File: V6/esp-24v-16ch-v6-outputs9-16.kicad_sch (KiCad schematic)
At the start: 5 parts, among them Q12 MMBT2222A

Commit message: V6 is up
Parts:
- R113: renamed from R112; Package 0402/1005 -> (none)
- R114: renamed from R113; value 1k -> 470R; LCSC Part # C11702 -> C25117; Mfr PN 0402WGF1001TCE -> 0402WGF4700TCE; Vendor PN C11702 -> C25117
- renumbered D65 to D66, R114 to R115
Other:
- note added: "I_{BASE} = (3.3V - V_{BE}) / 470R I_{BASE} = (3.3V - 0.7V) / 470R I_{BASE} = 5,53 mA ADEQUATE FOR FULL SATURATION OF THE TRANSISTOR UP TO I_{C} AROUND 550 mA CONSIDERING A FORCED BETA OF 10."

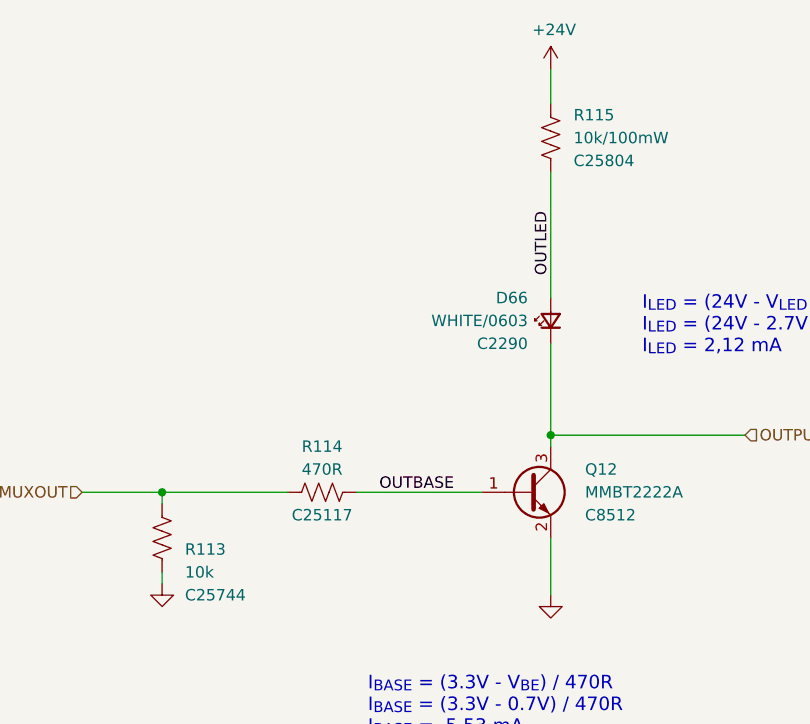
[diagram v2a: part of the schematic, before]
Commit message: Added voltage monitors for both ESP32 and LAN8710A
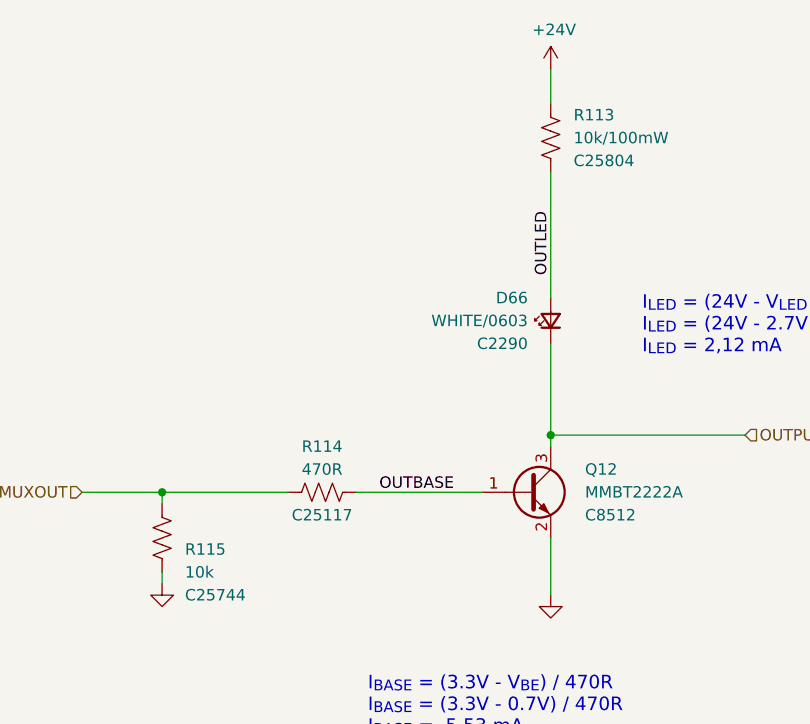
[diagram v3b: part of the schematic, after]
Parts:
- renumbered R115 to R113, R113 to R115
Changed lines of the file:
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@@
 		(title "ESP 24V 16xIn/16xOut/1-Wire Module")
 		(date "2026-02-10")
-		(rev "V6.0")
+		(rev "V6.0.3")
 	)
 	(text "RESISTORS: 62,5mW WHERE NOT SPECIFIED"
@@
 		(in_pos_files yes)
 		(dnp no)
-		(property "Reference" "#PWR0241"
+		(property "Reference" "#PWR0239"
 			(at 144.78 58.42 0)
 			(hide yes)
@@
 			(project "esp-24v-16ch-v6"
 				(path "/2bc5a21a-1d79-419d-a592-6852cc07b00a/118d8d95-c0ce-4d84-8406-4e7809444f6f"
-					(reference "#PWR0244")
+					(reference "#PWR0242")
 					(unit 1)
 				)
 				(path "/2bc5a21a-1d79-419d-a592-6852cc07b00a/18f82f59-0c23-40f7-8b4c-a32f0bda1493"
-					(reference "#PWR0262")
+					(reference "#PWR0260")
 					(unit 1)
 				)
 				(path "/2bc5a21a-1d79-419d-a592-6852cc07b00a/1c051e73-1175-469e-a364-cac197036f64"
-					(reference "#PWR0247")
+					(reference "#PWR0245")
 					(unit 1)
 				)
 				(path "/2bc5a21a-1d79-419d-a592-6852cc07b00a/58d16e81-f114-46b0-87d3-9324f007724a"
-					(reference "#PWR0241")
+					(reference "#PWR0239")
 					(unit 1)
 				)
 				(path "/2bc5a21a-1d79-419d-a592-6852cc07b00a/609d2beb-47a4-466a-8275-c7d831b810a1"
-					(reference "#PWR0250")
+					(reference "#PWR0248")
 					(unit 1)
 				)
 				(path "/2bc5a21a-1d79-419d-a592-6852cc07b00a/7ca24c0f-2468-4efa-8ee6-749df6aa5e15"
-					(reference "#PWR0259")
+					(reference "#PWR0257")
 					(unit 1)
 				)
 				(path "/2bc5a21a-1d79-419d-a592-6852cc07b00a/da3c2bc1-d321-4b0b-8d45-9bd0460c9e5a"
-					(reference "#PWR0253")
+					(reference "#PWR0251")
 					(unit 1)
 				)
 				(path "/2bc5a21a-1d79-419d-a592-6852cc07b00a/dbf038c9-8c09-4484-aee5-b965d923f833"
-					(reference "#PWR0256")
+					(reference "#PWR0254")
 					(unit 1)
 				)
@@
 		(in_pos_files yes)
 		(dnp no)
-		(property "Reference" "#PWR0242"
+		(property "Reference" "#PWR0241"
 			(at 144.78 119.38 0)
 			(hide yes)
@@
 			(project "esp-24v-16ch-v6"
 				(path "/2bc5a21a-1d79-419d-a592-6852cc07b00a/118d8d95-c0ce-4d84-8406-4e7809444f6f"
-					(reference "#PWR0245")
+					(reference "#PWR0244")
 					(unit 1)
 				)
 				(path "/2bc5a21a-1d79-419d-a592-6852cc07b00a/18f82f59-0c23-40f7-8b4c-a32f0bda1493"
-					(reference "#PWR0263")
+					(reference "#PWR0262")
 					(unit 1)
 				)
 				(path "/2bc5a21a-1d79-419d-a592-6852cc07b00a/1c051e73-1175-469e-a364-cac197036f64"
-					(reference "#PWR0248")
+					(reference "#PWR0247")
 					(unit 1)
 				)
 				(path "/2bc5a21a-1d79-419d-a592-6852cc07b00a/58d16e81-f114-46b0-87d3-9324f007724a"
-					(reference "#PWR0242")
+					(reference "#PWR0241")
 					(unit 1)
 				)
 				(path "/2bc5a21a-1d79-419d-a592-6852cc07b00a/609d2beb-47a4-466a-8275-c7d831b810a1"
-					(reference "#PWR0251")
+					(reference "#PWR0250")
 					(unit 1)
 				)
 				(path "/2bc5a21a-1d79-419d-a592-6852cc07b00a/7ca24c0f-2468-4efa-8ee6-749df6aa5e15"
-					(reference "#PWR0260")
+					(reference "#PWR0259")
 					(unit 1)
 				)
 				(path "/2bc5a21a-1d79-419d-a592-6852cc07b00a/da3c2bc1-d321-4b0b-8d45-9bd0460c9e5a"
-					(reference "#PWR0254")
+					(reference "#PWR0253")
 					(unit 1)
 				)
 				(path "/2bc5a21a-1d79-419d-a592-6852cc07b00a/dbf038c9-8c09-4484-aee5-b965d923f833"
-					(reference "#PWR0257")
+					(reference "#PWR0256")
 					(unit 1)
 				)
@@
 		(in_pos_files yes)
 		(dnp no)
-		(property "Reference" "R113"
+		(property "Reference" "R115"
 			(at 104.14 107.95 0)
 			(show_name no)
@@
 			(project "esp-24v-16ch-v6"
 				(path "/2bc5a21a-1d79-419d-a592-6852cc07b00a/118d8d95-c0ce-4d84-8406-4e7809444f6f"
-					(reference "R116")
+					(reference "R118")
 					(unit 1)
 				)
 				(path "/2bc5a21a-1d79-419d-a592-6852cc07b00a/18f82f59-0c23-40f7-8b4c-a32f0bda1493"
-					(reference "R134")
+					(reference "R136")
 					(unit 1)
 				)
 				(path "/2bc5a21a-1d79-419d-a592-6852cc07b00a/1c051e73-1175-469e-a364-cac197036f64"
-					(reference "R119")
+					(reference "R121")
 					(unit 1)
 				)
 				(path "/2bc5a21a-1d79-419d-a592-6852cc07b00a/58d16e81-f114-46b0-87d3-9324f007724a"
-					(reference "R113")
+					(reference "R115")
 					(unit 1)
 				)
 				(path "/2bc5a21a-1d79-419d-a592-6852cc07b00a/609d2beb-47a4-466a-8275-c7d831b810a1"
-					(reference "R122")
+					(reference "R124")
 					(unit 1)
 				)
 				(path "/2bc5a21a-1d79-419d-a592-6852cc07b00a/7ca24c0f-2468-4efa-8ee6-749df6aa5e15"
-					(reference "R131")
+					(reference "R133")
 					(unit 1)
 				)
 				(path "/2bc5a21a-1d79-419d-a592-6852cc07b00a/da3c2bc1-d321-4b0b-8d45-9bd0460c9e5a"
-					(reference "R125")
+					(reference "R127")
 					(unit 1)
 				)
 				(path "/2bc5a21a-1d79-419d-a592-6852cc07b00a/dbf038c9-8c09-4484-aee5-b965d923f833"
-					(reference "R128")
+					(reference "R130")
 					(unit 1)
 				)
@@
 		(in_pos_files yes)
 		(dnp no)
-		(property "Reference" "R115"
+		(property "Reference" "R113"
 			(at 147.32 59.69 0)
 			(show_name no)
@@
 			(project "esp-24v-16ch-v6"
 				(path "/2bc5a21a-1d79-419d-a592-6852cc07b00a/118d8d95-c0ce-4d84-8406-4e7809444f6f"
-					(reference "R118")
+					(reference "R116")
 					(unit 1)
 				)
 				(path "/2bc5a21a-1d79-419d-a592-6852cc07b00a/18f82f59-0c23-40f7-8b4c-a32f0bda1493"
-					(reference "R136")
+					(reference "R134")
 					(unit 1)
 				)
 				(path "/2bc5a21a-1d79-419d-a592-6852cc07b00a/1c051e73-1175-469e-a364-cac197036f64"
-					(reference "R121")
+					(reference "R119")
 					(unit 1)
 				)
 				(path "/2bc5a21a-1d79-419d-a592-6852cc07b00a/58d16e81-f114-46b0-87d3-9324f007724a"
-					(reference "R115")
+					(reference "R113")
 					(unit 1)
 				)
 				(path "/2bc5a21a-1d79-419d-a592-6852cc07b00a/609d2beb-47a4-466a-8275-c7d831b810a1"
-					(reference "R124")
+					(reference "R122")
 					(unit 1)
 				)
 				(path "/2bc5a21a-1d79-419d-a592-6852cc07b00a/7ca24c0f-2468-4efa-8ee6-749df6aa5e15"
-					(reference "R133")
+					(reference "R131")
 					(unit 1)
 				)
 				(path "/2bc5a21a-1d79-419d-a592-6852cc07b00a/da3c2bc1-d321-4b0b-8d45-9bd0460c9e5a"
-					(reference "R127")
+					(reference "R125")
 					(unit 1)
 				)
 				(path "/2bc5a21a-1d79-419d-a592-6852cc07b00a/dbf038c9-8c09-4484-aee5-b965d923f833"
-					(reference "R130")
-					(unit 1)
-				)
+					(reference "R128")
+					(unit 1)
+				)
